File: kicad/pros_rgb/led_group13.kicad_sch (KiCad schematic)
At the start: 8 parts

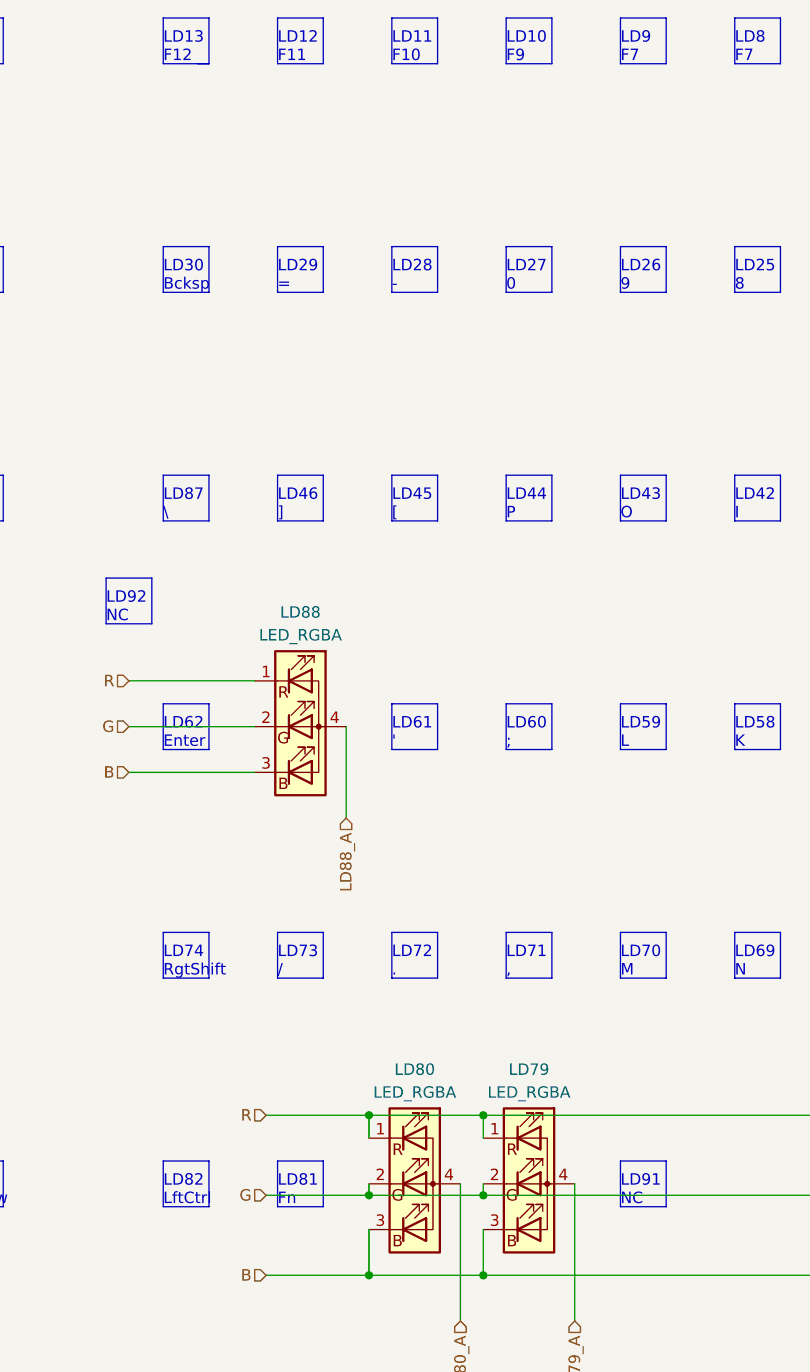
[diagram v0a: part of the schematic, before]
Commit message: kicad/pros_rgb: fix typos
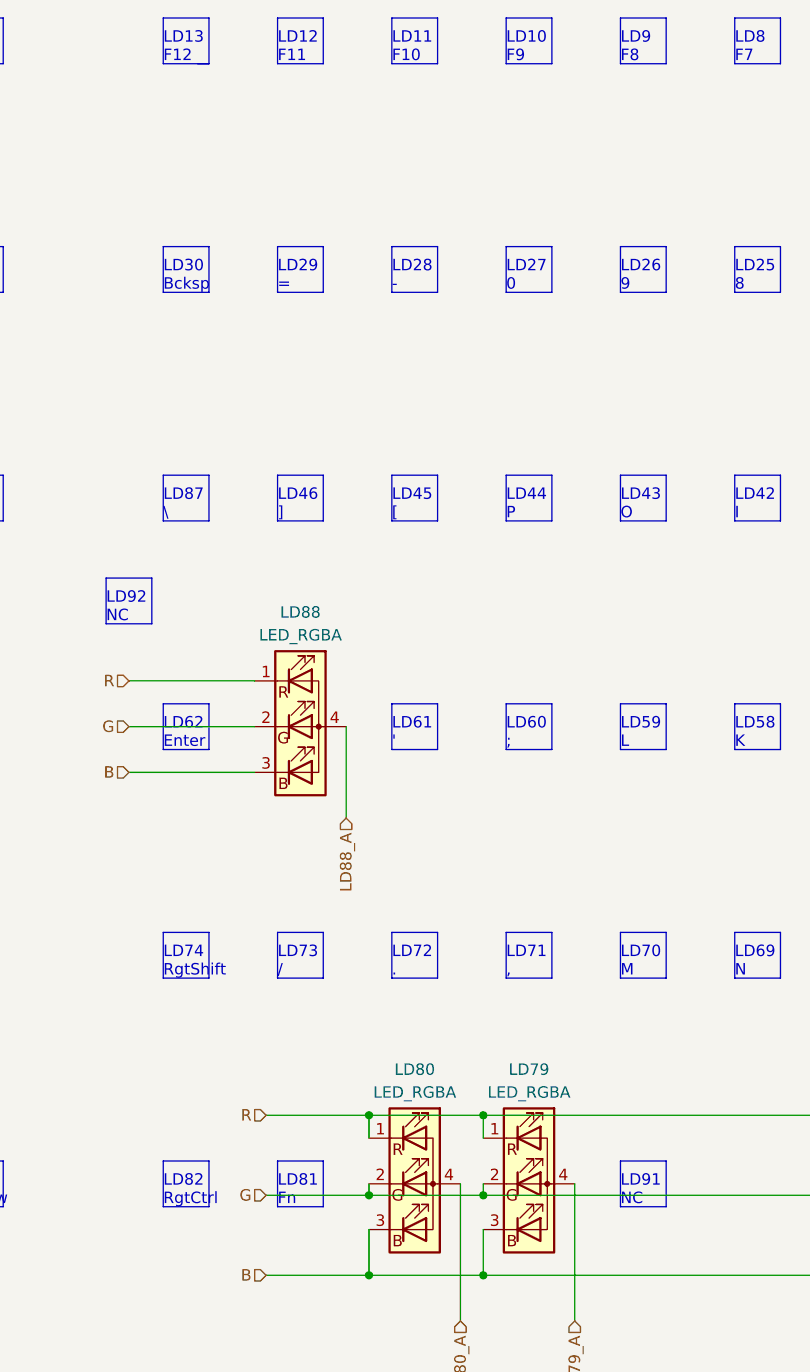
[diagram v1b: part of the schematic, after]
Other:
- note added: "LD82 RgtCtrl"
- note added: "LD9 F8"
- note removed: "LD82 LftCtrl"
- note removed: "LD9 F7"
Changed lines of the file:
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@@
     (effects (font (size 1.27 1.27)) (justify left bottom))
   )
-  (text "LD82\nLftCtrl" (at 106.68 156.21 0)
+  (text "LD82\nRgtCtrl" (at 106.68 156.21 0)
     (effects (font (size 1.27 1.27)) (justify left bottom))
   )
@@
     (effects (font (size 1.27 1.27)) (justify left bottom))
   )
-  (text "LD9\nF7" (at 157.48 29.21 0)
+  (text "LD9\nF8" (at 157.48 29.21 0)
     (effects (font (size 1.27 1.27)) (justify left bottom))
   )

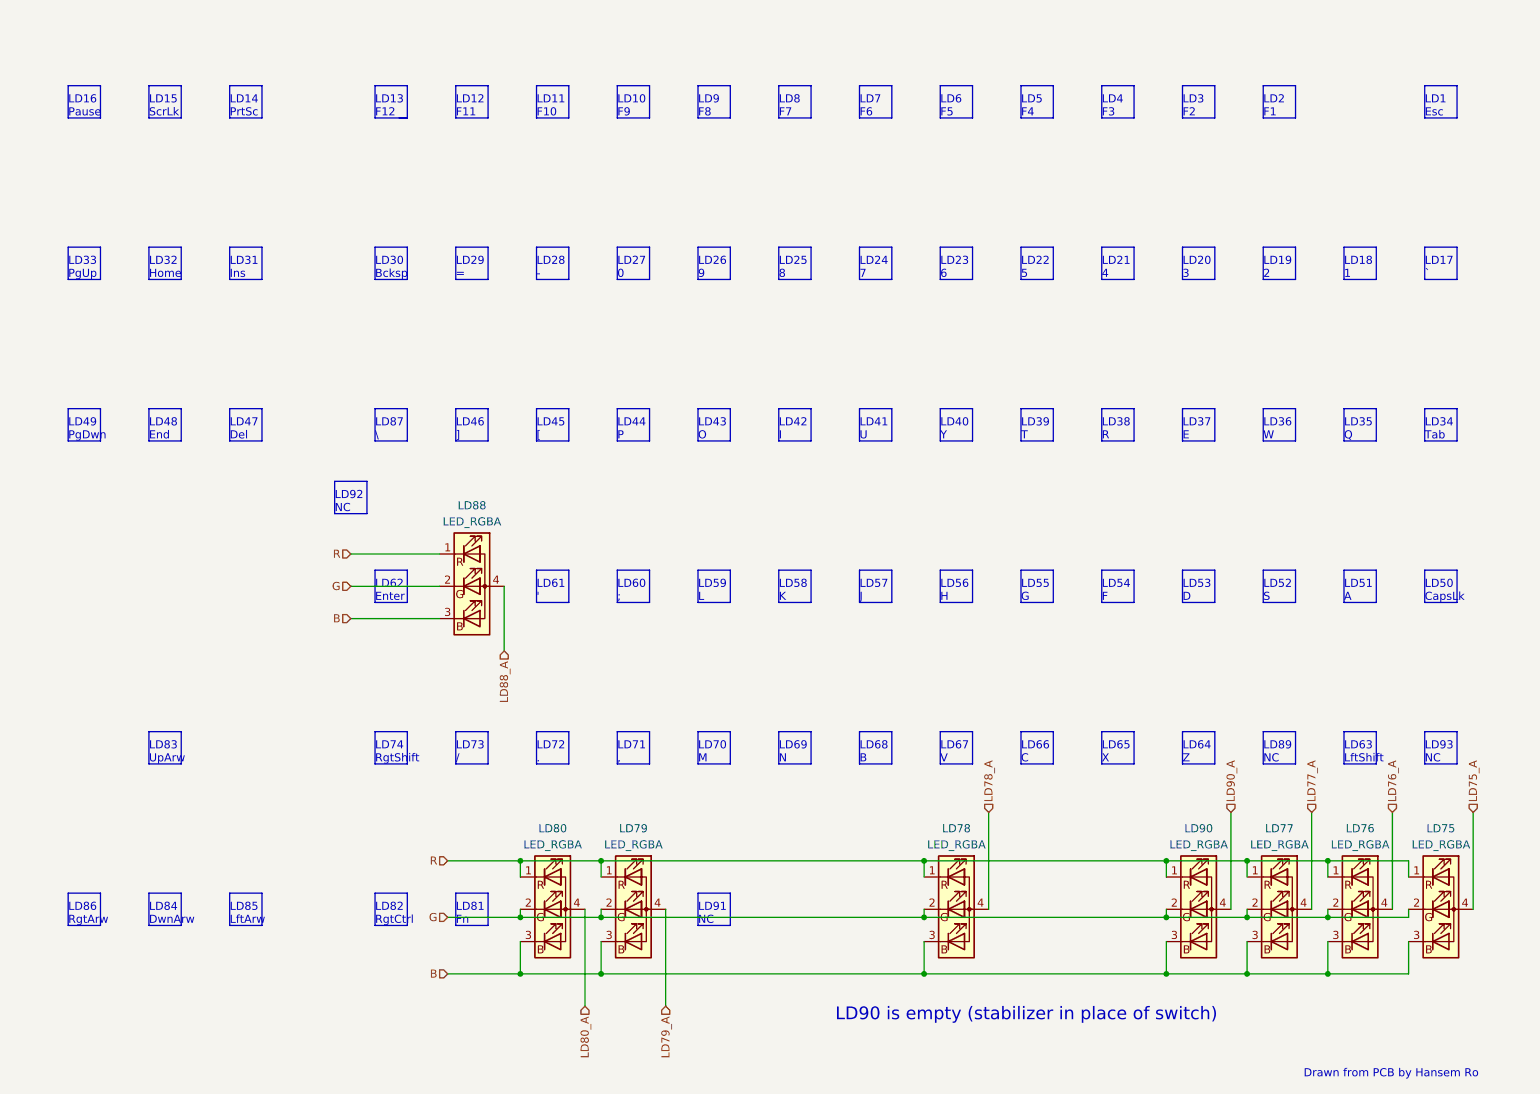
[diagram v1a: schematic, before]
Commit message: kicad/pros_rgb: order led groups by channel number
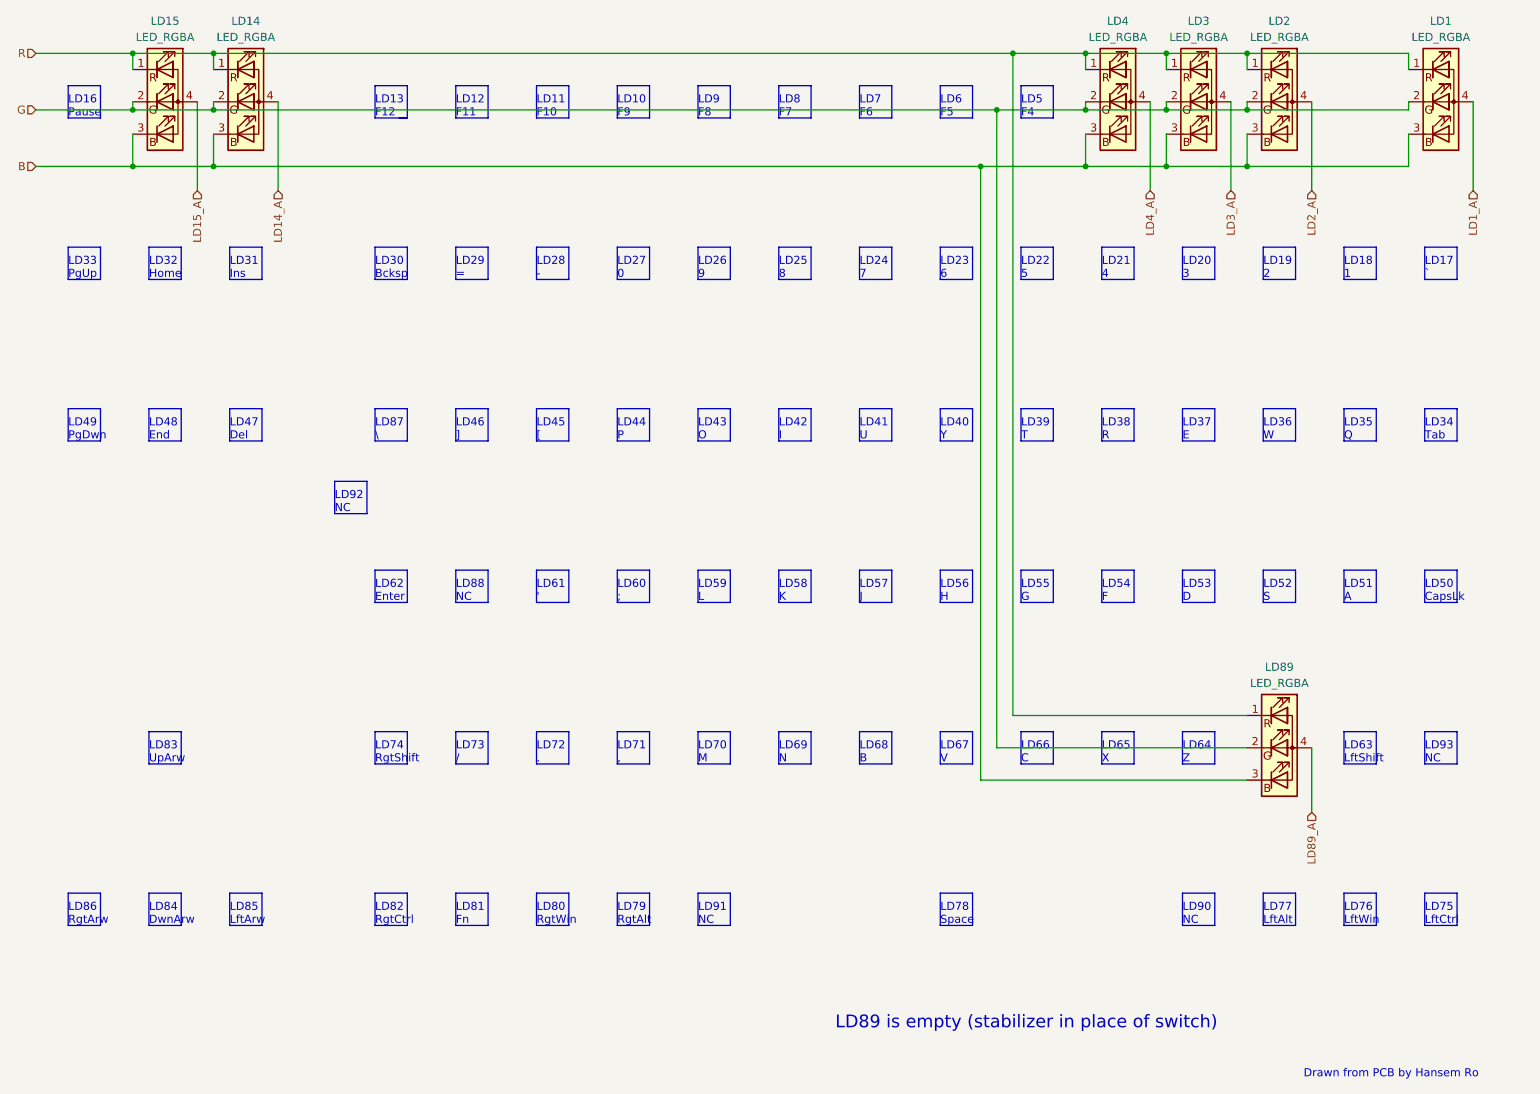
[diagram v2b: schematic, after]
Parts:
- removed LD75, LD76, LD77, LD78, LD79, LD80, LD88, LD90: LED_RGBA, symbol Device:LED_RGBA
- added LD1, LD14, LD15, LD2, LD3, LD4, LD89: LED_RGBA, symbol Device:LED_RGBA
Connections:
- net B: now also LD1.3 (BK), LD14.3 (BK), LD15.3 (BK), LD2.3 (BK), LD3.3 (BK), LD4.3 (BK), LD89.3 (BK)
- net G: now also LD1.2 (GK), LD14.2 (GK), LD15.2 (GK), LD2.2 (GK), LD3.2 (GK), LD4.2 (GK), LD89.2 (GK)
- net R: now also LD1.1 (RK), LD14.1 (RK), LD15.1 (RK), LD2.1 (RK), LD3.1 (RK), LD4.1 (RK), LD89.1 (RK)
- new net LD14_A: LD14.4 (A)
- new net LD15_A: LD15.4 (A)
- new net LD1_A: LD1.4 (A)
- new net LD2_A: LD2.4 (A)
- new net LD3_A: LD3.4 (A)
- new net LD4_A: LD4.4 (A)
- new net LD89_A: LD89.4 (A)
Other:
- note added: "LD75 LftCtrl"
- note added: "LD76 LftWin"
- note added: "LD77 LftAlt"
- note added: "LD78 Space"
- note added: "LD79 RgtAlt"
- note added: "LD80 RgtWin"
- note added: "LD88 NC"
- note added: "LD89 is empty (stabilizer in place of switch)"
- note added: "LD90 NC"
- note removed: "LD1 Esc"
- note removed: "LD14 PrtSc"
- note removed: "LD15 ScrLk"
- note removed: "LD2 F1"
- note removed: "LD3 F2"
- note removed: "LD4 F3"
- note removed: "LD89 NC"
- note removed: "LD90 is empty (stabilizer in place of switch)"
